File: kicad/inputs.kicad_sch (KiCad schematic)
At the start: 11 parts, among them J5 Thonkiconn, U5 MCP3208, U5 MCP6002-xSN

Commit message: make 4hp
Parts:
- added C9: 100n, Capacitor_SMD:C_0402_1005Metric, symbol Device:C
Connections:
- net +3V3: now also C9.1
- net Earth: now also C9.2
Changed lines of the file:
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@@
   (junction (at 101.6 52.07) (diameter 0) (color 0 0 0 0)
   )
+  (junction (at 179.07 100.33) (diameter 0) (color 0 0 0 0)
+  )
+  (junction (at 179.07 72.39) (diameter 0) (color 0 0 0 0)
+  )
   (junction (at 69.85 49.53) (diameter 0) (color 0 0 0 0)
   )
@@
     (stroke (width 0) (type default))
   )
+  (wire (pts (xy 210.82 72.39) (xy 179.07 72.39))
+    (stroke (width 0) (type default))
+  )
   (wire (pts (xy 101.6 52.07) (xy 99.06 52.07))
     (stroke (width 0) (type default))
   )
+  (wire (pts (xy 210.82 82.55) (xy 210.82 72.39))
+    (stroke (width 0) (type default))
+  )
   (wire (pts (xy 101.6 102.87) (xy 123.19 102.87))
     (stroke (width 0) (type default))
@@
     (stroke (width 0) (type default))
   )
+  (wire (pts (xy 210.82 100.33) (xy 210.82 90.17))
+    (stroke (width 0) (type default))
+  )
   (wire (pts (xy 52.07 49.53) (xy 62.23 49.53))
     (stroke (width 0) (type default))
@@
   )
   (wire (pts (xy 83.82 105.41) (xy 81.28 105.41))
+    (stroke (width 0) (type default))
+  )
+  (wire (pts (xy 179.07 100.33) (xy 210.82 100.33))
     (stroke (width 0) (type default))
   )
@@
         )
       )
+    )
+  )
+  (symbol (lib_id "Device:C") (at 210.82 86.36 0) (unit 1)
+    (in_bom yes) (on_board yes) (dnp no) (fields_autoplaced)
+    (property "Reference" "C9" (at 214.63 85.725 0)
+      (effects (font (size 1.27 1.27)) (justify left))
+    )
+    (property "Value" "100n" (at 214.63 88.265 0)
+      (effects (font (size 1.27 1.27)) (justify left))
+    )
+    (property "Footprint" "Capacitor_SMD:C_0402_1005Metric" (at 211.7852 90.17 0)
+      (effects (font (size 1.27 1.27)) hide)
+    )
+    (property "Datasheet" "~" (at 210.82 86.36 0)
+      (effects (font (size 1.27 1.27)) hide)
+    )
+    (property "JLC" "C307331" (at 210.82 86.36 0)
+      (effects (font (size 1.27 1.27)) hide)
+    )
+    (pin "1")
+    (pin "2")
+    (instances
+      (project "EuroPi-LC"
+        (path "/0909364c-8c17-4313-9980-e4080dc21894"
+          (reference "C9") (unit 1)
+        )
+        (path "/0909364c-8c17-4313-9980-e4080dc21894/dda9adb9-cb69-4d89-a036-80e6705a55b4"
+          (reference "C24") (unit 1)
+        )
+      )
+      (project "EuroPi LC"
+        (path "/1702e620-a749-4340-9e49-cfdb2636cab7/8b492937-b70b-4e04-a312-87c396a83887"
+          (reference "C12") (unit 1)
+        )
+      )
+      (project "rp2040-core"
+        (path "/925c7a06-03f3-41da-8f05-8de1ef6b1e44"
+          (reference "C9") (unit 1)
+        )
+      )

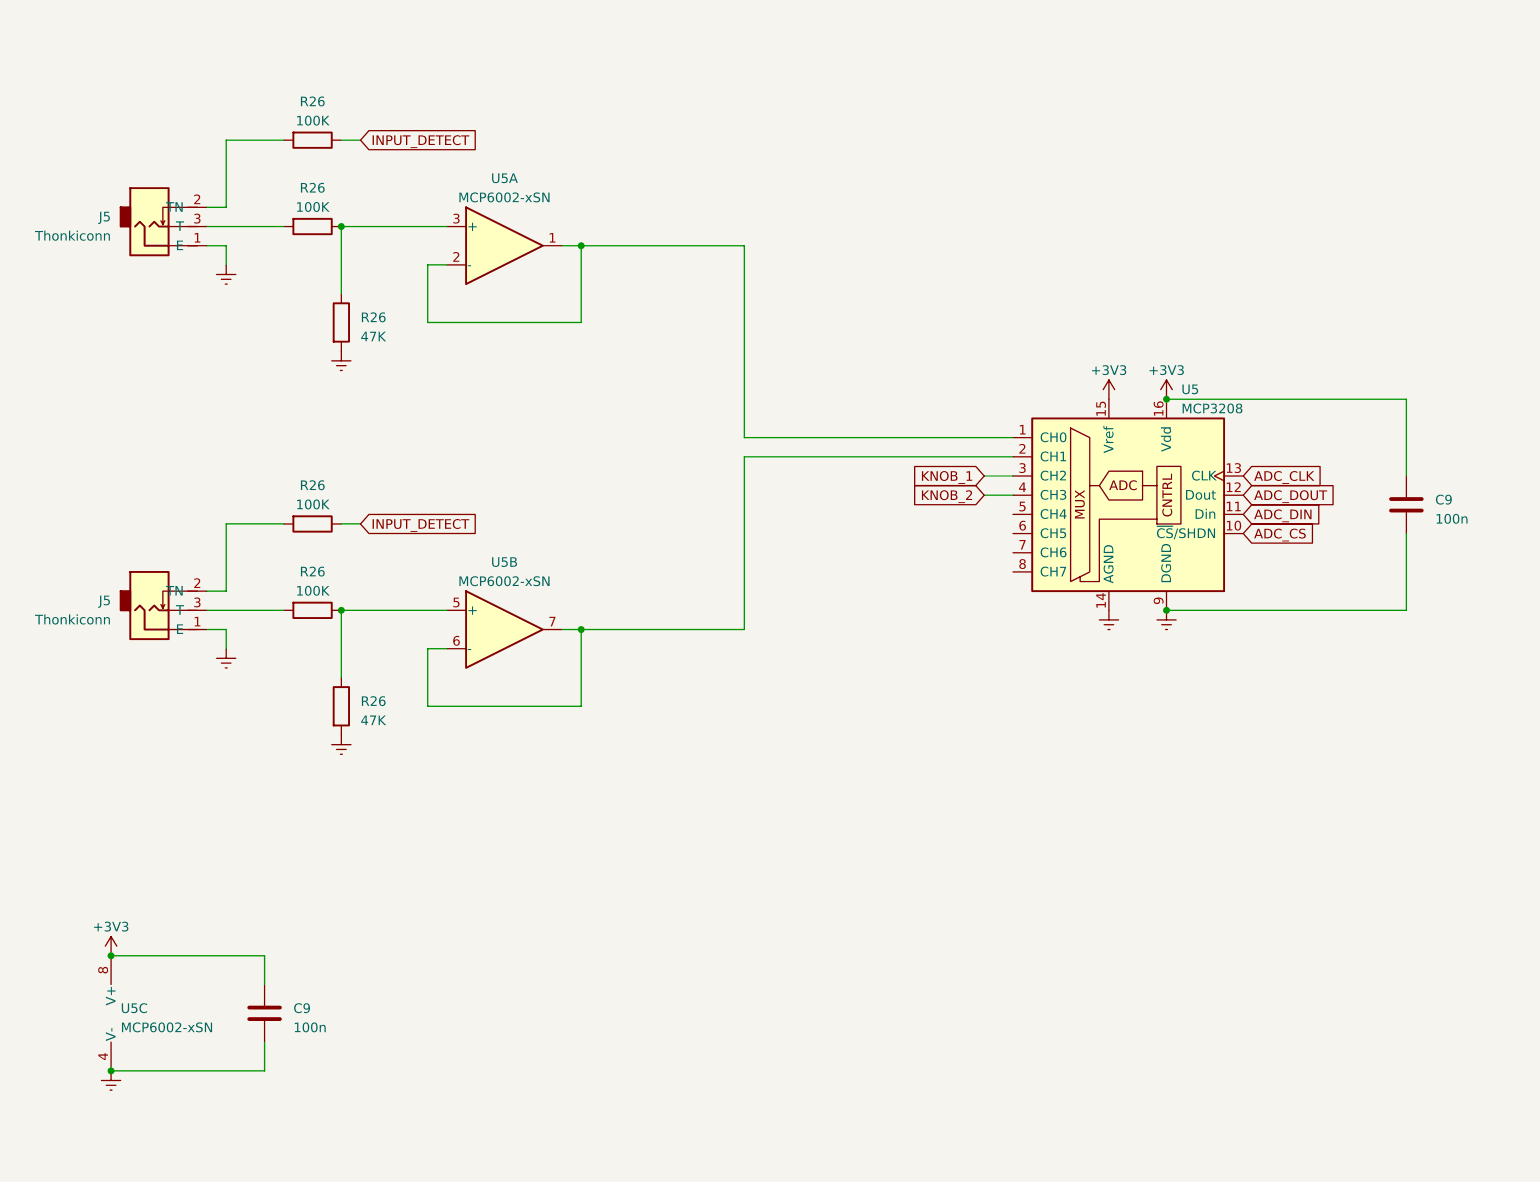
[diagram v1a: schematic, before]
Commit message: input changes
use single channel ADCs for analog inputs and knob 1 which use i2c instead of SPI to free up one pin for input 1 to be used as a digital input as well
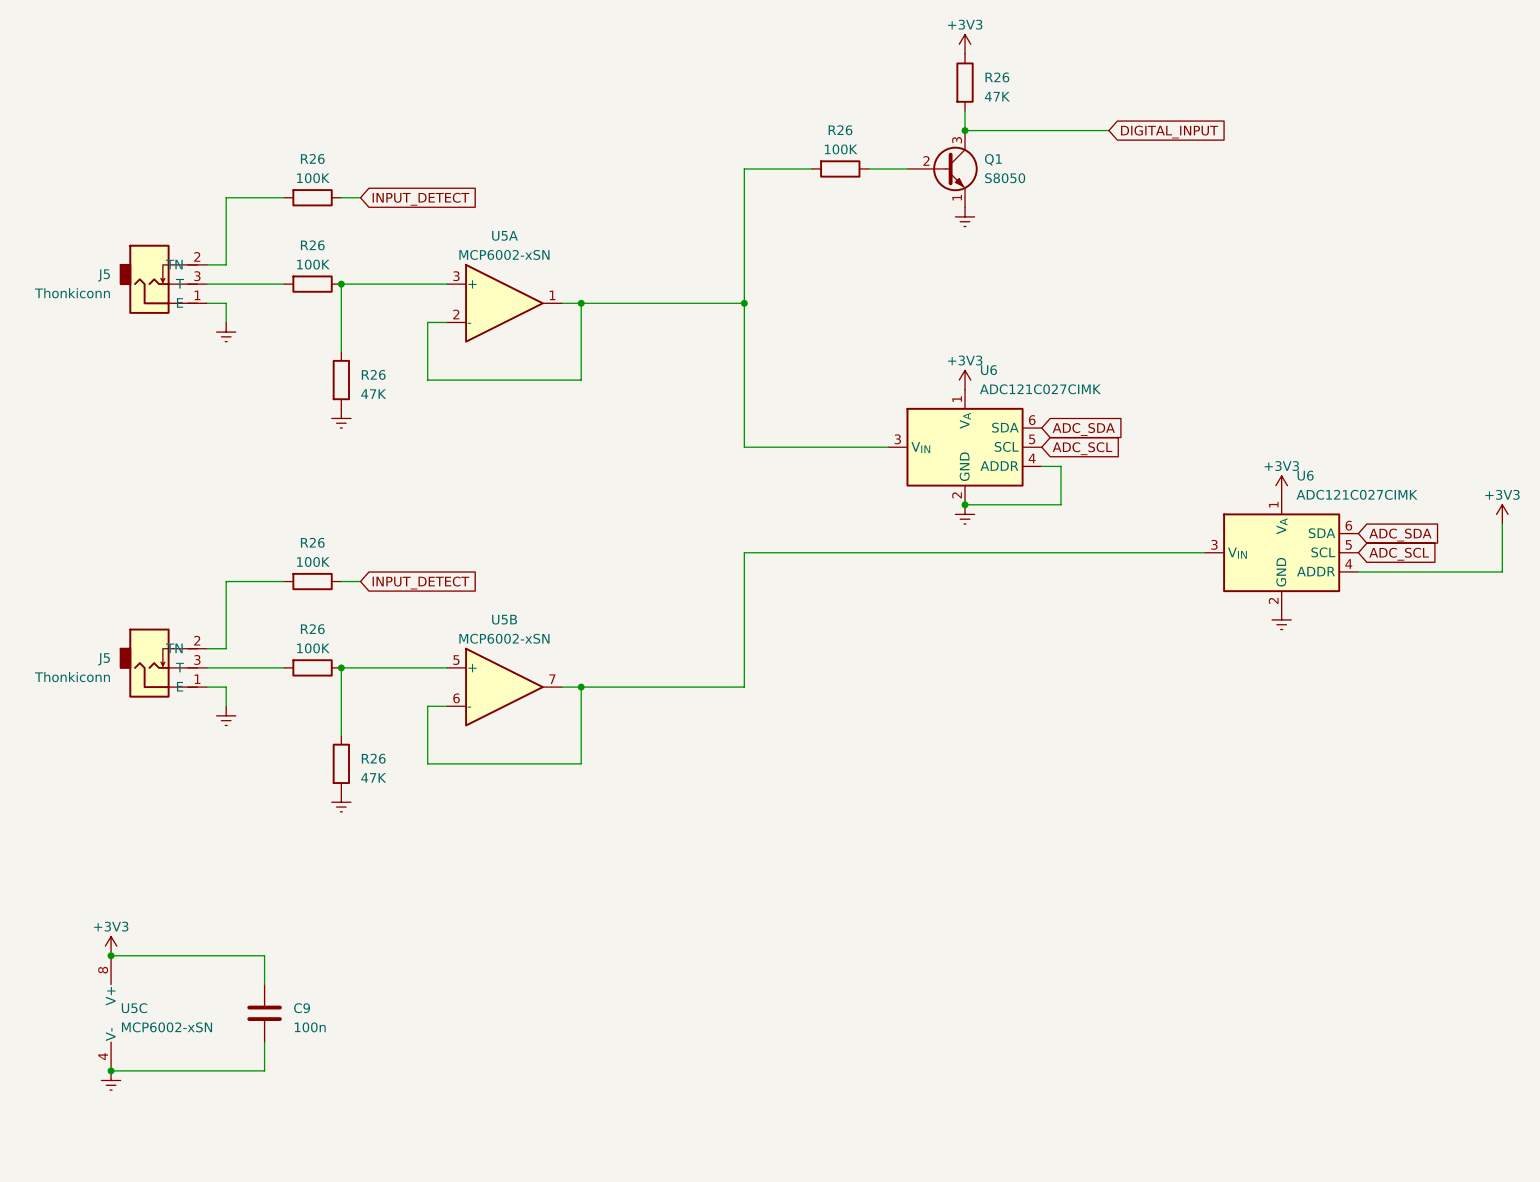
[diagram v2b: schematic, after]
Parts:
- removed C9: 100n, Capacitor_SMD:C_0402_1005Metric, symbol Device:C
- removed U5: MCP3208, Package_SO:SOIC-16_3.9x9.9mm_P1.27mm, symbol Analog_ADC:MCP3208
- added Q1: S8050, Package_TO_SOT_SMD:SOT-23, symbol Transistor_BJT:S8050
- added R26: 100K, Resistor_SMD:R_0402_1005Metric, symbol Device:R
- added R26: 47K, Resistor_SMD:R_0402_1005Metric, symbol Device:R
- added U6 (x2): ADC121C027CIMK, Package_TO_SOT_SMD:TSOT-23-6, symbol Analog_ADC:ADC101C021CIMK
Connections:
- net +3V3: now also R26.1, U6.1 (V_{A}), U6.1 (V_{A}), U6.4 (ADDR)
- net Earth: now also Q1.1 (E), U6.2 (GND), U6.2 (GND), U6.4 (ADDR)
- net at U5.1, U5.2 (-): now also R26.2, U6.3 (V_{IN})
- net at U5.6 (-), U5.7: now also U6.3 (V_{IN})
- new net: Q1.2 (B), R26.1
- new net ADC_SCL: U6.5 (SCL), U6.5 (SCL)
- new net ADC_SDA: U6.6 (SDA), U6.6 (SDA)
- new net DIGITAL_INPUT: Q1.3 (C), R26.2
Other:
- moved on the sheet: J5, R26, U5A, U5B

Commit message: reroute pcb
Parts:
- J5: footprint Eurorack:Thonkiconn Mono Jack -> allen-synthesis:jack-thonkiconn-mono
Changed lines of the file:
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@@
       (effects (font (size 1.27 1.27)) (justify right))
     )
-    (property "Footprint" "Eurorack:Thonkiconn Mono Jack" (at 41.91 111.76 0)
+    (property "Footprint" "allen-synthesis:jack-thonkiconn-mono" (at 41.91 111.76 0)
       (effects (font (size 1.27 1.27)) hide)
     )
@@
       (effects (font (size 1.27 1.27)) (justify right))
     )
-    (property "Footprint" "Eurorack:Thonkiconn Mono Jack" (at 41.91 60.96 0)
-      (effects (font (size 1.27 1.27)) hide)
-    )
+    (property "Footprint" "allen-synthesis:jack-thonkiconn-mono" (at 41.91 60.96 0)
+      (effects (font (size 1.27 1.27)) hide)
+    )

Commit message: add schematic notes
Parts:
- added C9 (x2): 100n, Capacitor_SMD:C_0402_1005Metric, symbol Device:C
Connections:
- net +3V3: now also C9.1, C9.1
- net Earth: now also C9.2, C9.2
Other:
- note added: "The I2C ADCs accept a 0-3.3V input. They accept a tristate address input, so the 3 used are wired differently; one to ground, one to +3.3V, and one left floating"
- note added: "The digital input is connected to the output of the op-amp to prevent it from interfering with the signal before the buffer. This also means it's threshold is higher as the signal is attenuated first, resulting in a lower chance of false triggering. Threshold ~2V"
- note added: "The input detect signal is connected to the jack via a 100k resistor to prevent it from interfering but still allowing a signal to be sent to the jack to simulate a signal"
- note added: "The input is attenuated by ~0.32x to convert 0-10V into 0-3.2V to allow it to be read by the 3.3V ADC with a small amount of headroom. It's then buffered using an op-amp to reduce impedance issues and to clip the signal to 0-3.3V in the event of negative voltage input"
- moved on the sheet: C9, J5, R26, U5B, U5C, U6
